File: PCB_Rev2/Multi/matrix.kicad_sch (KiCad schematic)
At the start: 126 parts

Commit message: Add ISO Support
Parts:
- added D54: DIODE, Diode_SMD:D_SOD-123, symbol Device:D
- added S54: MX1A, PCM_Switch_Keyboard_Hotswap_Kailh:SW_Hotswap_Kailh_MX_Plated_1.00u, symbol Switch:SW_Push
- S29: footprint PCM_Switch_Keyboard_Hotswap_Kailh:SW_Hotswap_Kailh_MX_Plated_1.75u -> PCM_Switch_Keyboard_Hotswap_Kailh:SW_Hotswap_Kailh_MX_Plated_1.75u_90deg
- S55, S56, S57, S60, S61, S62: footprint PCM_Switch_Keyboard_Hotswap_Kailh:SW_Hotswap_Kailh_MX_Plated_1.25u -> PCM_Switch_Keyboard_Hotswap_Kailh:SW_Hotswap_Kailh_MX_Plated_1.25u_90deg
- renumbered D54 to D55, D55 to D56, S54 to S55, S55 to S56
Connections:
- net col_11: now also S54.2
- net row_3: now also D54.1 (K)
- new net: D54.2 (A), S54.1
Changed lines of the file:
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@@
 	)
 	(junction
+		(at 332.74 125.73)
+		(diameter 0)
+		(color 0 0 0 0)
+	)
+	(junction
 		(at 332.74 60.96)
 		(diameter 0)
@@
 	)
 	(junction
+		(at 322.58 135.89)
+		(diameter 0)
+		(color 0 0 0 0)
+	)
+	(junction
 		(at 307.34 104.14)
 		(diameter 0)
@@
 	(wire
 		(pts
-			(xy 297.18 135.89) (xy 347.98 135.89)
+			(xy 297.18 135.89) (xy 322.58 135.89)
 		)
 		(stroke
@@
 	(wire
 		(pts
+			(xy 322.58 135.89) (xy 347.98 135.89)
+		)
+		(stroke
+			(width 0)
+			(type default)
+		)
+	)
+	(wire
+		(pts
 			(xy 205.74 60.96) (xy 205.74 82.55)
 		)
@@
 	(wire
 		(pts
-			(xy 332.74 104.14) (xy 332.74 147.32)
+			(xy 332.74 104.14) (xy 332.74 125.73)
 		)
 		(stroke
@@
 	(wire
 		(pts
+			(xy 322.58 134.62) (xy 322.58 135.89)
+		)
+		(stroke
+			(width 0)
+			(type default)
+		)
+	)
+	(wire
+		(pts
 			(xy 307.34 60.96) (xy 307.34 82.55)
 		)
@@
 	(wire
 		(pts
+			(xy 322.58 125.73) (xy 322.58 127)
+		)
+		(stroke
+			(width 0)
+			(type default)
+		)
+	)
+	(wire
+		(pts
 			(xy 322.58 71.12) (xy 347.98 71.12)
 		)
@@
 	(wire
 		(pts
+			(xy 332.74 125.73) (xy 332.74 147.32)
+		)
+		(stroke
+			(width 0)
+			(type default)
+		)
+	)
+	(wire
+		(pts
 			(xy 93.98 69.85) (xy 93.98 71.12)
 		)
@@
 			(project "PH60"
 				(path "/dca0f898-8fdb-4522-a51d-f4f4238906e7/dc5cd3b2-ef82-41de-b720-71645d542746"
-					(reference "D63")
+					(reference "D64")
 					(unit 1)
 				)
@@
 			(project "PH60"
 				(path "/dca0f898-8fdb-4522-a51d-f4f4238906e7/dc5cd3b2-ef82-41de-b720-71645d542746"
-					(reference "D57")
+					(reference "D58")
 					(unit 1)
 				)
@@
 			(project "PH60"
 				(path "/dca0f898-8fdb-4522-a51d-f4f4238906e7/dc5cd3b2-ef82-41de-b720-71645d542746"
-					(reference "D61")
+					(reference "D62")
 					(unit 1)
 				)
@@
 			(project "PH60"
 				(path "/dca0f898-8fdb-4522-a51d-f4f4238906e7/dc5cd3b2-ef82-41de-b720-71645d542746"
-					(reference "D59")
+					(reference "D60")
 					(unit 1)
 				)
@@
 			(project "PH60"
 				(path "/dca0f898-8fdb-4522-a51d-f4f4238906e7/dc5cd3b2-ef82-41de-b720-71645d542746"
-					(reference "S59")
+					(reference "S60")
 					(unit 1)
 				)
@@
 			)
 		)
-		(property "Footprint" "PCM_Switch_Keyboard_Hotswap_Kailh:SW_Hotswap_Kailh_MX_Plated_1.25u"
+		(property "Footprint" "PCM_Switch_Keyboard_Hotswap_Kailh:SW_Hotswap_Kailh_MX_Plated_1.25u_90deg"
 			(at 99.06 152.4 0)
 			(effects
@@
 			(project "PH60"
 				(path "/dca0f898-8fdb-4522-a51d-f4f4238906e7/dc5cd3b2-ef82-41de-b720-71645d542746"
-					(reference "S58")
+					(reference "S59")
 					(unit 1)
 				)
@@
 		(dnp no)
 		(fields_autoplaced yes)
-		(property "Reference" "S54"
+		(property "Reference" "S55"
 			(at 353.06 120.65 0)
 			(effects
@@
 			(project "PH60_Rev3"
 				(path "/dca0f898-8fdb-4522-a51d-f4f4238906e7/dc5cd3b2-ef82-41de-b720-71645d542746"
-					(reference "S54")
+					(reference "S55")
 					(unit 1)
 				)
@@
 			(project "PH60"
 				(path "/dca0f898-8fdb-4522-a51d-f4f4238906e7/dc5cd3b2-ef82-41de-b720-71645d542746"
-					(reference "D62")
+					(reference "D63")
 					(unit 1)
 				)
@@
 			)
 		)
-		(property "Footprint" "PCM_Switch_Keyboard_Hotswap_Kailh:SW_Hotswap_Kailh_MX_Plated_1.25u"
+		(property "Footprint" "PCM_Switch_Keyboard_Hotswap_Kailh:SW_Hotswap_Kailh_MX_Plated_1.25u_90deg"
 			(at 353.06 152.4 0)
 			(effects
@@
 			(project "PH60"
 				(path "/dca0f898-8fdb-4522-a51d-f4f4238906e7/dc5cd3b2-ef82-41de-b720-71645d542746"
-					(reference "S62")
+					(reference "S63")
 					(unit 1)
 				)
@@
 			(project "PH60"
 				(path "/dca0f898-8fdb-4522-a51d-f4f4238906e7/dc5cd3b2-ef82-41de-b720-71645d542746"
-					(reference "D60")
+					(reference "D61")
 					(unit 1)
 				)
@@
 			(project "PH60"
 				(path "/dca0f898-8fdb-4522-a51d-f4f4238906e7/dc5cd3b2-ef82-41de-b720-71645d542746"
-					(reference "S60")
+					(reference "S61")
 					(unit 1)
 				)
@@
 			)
 		)
-		(property "Footprint" "PCM_Switch_Keyboard_Hotswap_Kailh:SW_Hotswap_Kailh_MX_Plated_1.25u"
+		(property "Footprint" "PCM_Switch_Keyboard_Hotswap_Kailh:SW_Hotswap_Kailh_MX_Plated_1.25u_90deg"
 			(at 73.66 152.4 0)
 			(effects
@@
 			(project "PH60"
 				(path "/dca0f898-8fdb-4522-a51d-f4f4238906e7/dc5cd3b2-ef82-41de-b720-71645d542746"
-					(reference "S57")
+					(reference "S58")
 					(unit 1)
 				)
@@
 		(dnp no)
 		(fields_autoplaced yes)
-		(property "Reference" "D54"
+		(property "Reference" "D55"
 			(at 350.52 129.5399 90)
 			(effects
@@
 			(project "PH60_Rev3"
 				(path "/dca0f898-8fdb-4522-a51d-f4f4238906e7/dc5cd3b2-ef82-41de-b720-71645d542746"
-					(reference "D54")
+					(reference "D55")
 					(unit 1)
 				)
@@
 			)
 		)
-		(property "Footprint" "PCM_Switch_Keyboard_Hotswap_Kailh:SW_Hotswap_Kailh_MX_Plated_1.25u"
+		(property "Footprint" "PCM_Switch_Keyboard_Hotswap_Kailh:SW_Hotswap_Kailh_MX_Plated_1.25u_90deg"
 			(at 48.26 152.4 0)
 			(effects
@@
 			(project "PH60"
 				(path "/dca0f898-8fdb-4522-a51d-f4f4238906e7/dc5cd3b2-ef82-41de-b720-71645d542746"
-					(reference "S56")
+					(reference "S57")
 					(unit 1)
 				)
@@
 			)
 		)
-		(property "Footprint" "PCM_Switch_Keyboard_Hotswap_Kailh:SW_Hotswap_Kailh_MX_Plated_1.25u"
+		(property "Footprint" "PCM_Switch_Keyboard_Hotswap_Kailh:SW_Hotswap_Kailh_MX_Plated_1.25u_90deg"
 			(at 378.46 152.4 0)
 			(effects
@@
 			(project "PH60"
 				(path "/dca0f898-8fdb-4522-a51d-f4f4238906e7/dc5cd3b2-ef82-41de-b720-71645d542746"
-					(reference "S63")
+					(reference "S64")
 					(unit 1)
 				)
@@
 		(dnp no)
 		(fields_autoplaced yes)
-		(property "Reference" "S55"
+		(property "Reference" "S56"
 			(at 378.46 120.65 0)
 			(effects
@@
 			(project "PH60_Rev3"
 				(path "/dca0f898-8fdb-4522-a51d-f4f4238906e7/dc5cd3b2-ef82-41de-b720-71645d542746"
-					(reference "S55")
+					(reference "S56")
 					(unit 1)
 				)
@@
 			(project "PH60"
 				(path "/dca0f898-8fdb-4522-a51d-f4f4238906e7/dc5cd3b2-ef82-41de-b720-71645d542746"
-					(reference "D56")
+					(reference "D57")
 					(unit 1)
 				)
@@
 			)
 		)
-		(property "Footprint" "PCM_Switch_Keyboard_Hotswap_Kailh:SW_Hotswap_Kailh_MX_Plated_1.75u"
+		(property "Footprint" "PCM_Switch_Keyboard_Hotswap_Kailh:SW_Hotswap_Kailh_MX_Plated_1.75u_90deg"
 			(at 48.26 109.22 0)
 			(effects
@@
 			)
 		)
-		(property "Footprint" "PCM_Switch_Keyboard_Hotswap_Kailh:SW_Hotswap_Kailh_MX_Plated_1.25u"
+		(property "Footprint" "PCM_Switch_Keyboard_Hotswap_Kailh:SW_Hotswap_Kailh_MX_Plated_1.25u_90deg"
 			(at 327.66 152.4 0)
 			(effects
@@
 			(project "PH60"
 				(path "/dca0f898-8fdb-4522-a51d-f4f4238906e7/dc5cd3b2-ef82-41de-b720-71645d542746"
-					(reference "S61")
+					(reference "S62")
 					(unit 1)
 				)
@@
 		(dnp no)
 		(fields_autoplaced yes)
-		(property "Reference" "D55"
+		(property "Reference" "D56"
 			(at 375.92 129.5399 90)
 			(effects
@@
 			(project "PH60_Rev3"
 				(path "/dca0f898-8fdb-4522-a51d-f4f4238906e7/dc5cd3b2-ef82-41de-b720-71645d542746"
-					(reference "D55")
+					(reference "D56")
 					(unit 1)
 				)
@@
 			(project "PH60"
 				(path "/dca0f898-8fdb-4522-a51d-f4f4238906e7/dc5cd3b2-ef82-41de-b720-71645d542746"
-					(reference "D58")
+					(reference "D59")
+					(unit 1)
+				)
+			)
+		)
+	)
+	(symbol
+		(lib_id "Device:D")
+		(at 322.58 130.81 90)
+		(unit 1)
+		(exclude_from_sim no)
+		(in_bom yes)
+		(on_board yes)
+		(dnp no)
+		(fields_autoplaced yes)
+		(property "Reference" "D54"
+			(at 325.12 129.5399 90)
+			(effects
+				(font
+					(size 1.016 1.016)
+				)
+				(justify right)
+			)
+		)
+		(property "Value" "DIODE"
+			(at 325.12 132.0799 90)
+			(effects
+				(font
+					(size 1.016 1.016)
+				)
+				(justify right)
+			)
+		)
+		(property "Footprint" "Diode_SMD:D_SOD-123"
+			(at 322.58 130.81 0)
+			(effects
+				(font
+					(size 1.27 1.27)
+				)
+				(hide yes)
+			)
+		)
+		(property "Datasheet" "~"
+			(at 322.58 130.81 0)
+			(effects
+				(font
+					(size 1.27 1.27)
+				)
+				(hide yes)
+			)
+		)
+		(property "Description" "Diode"
+			(at 322.58 130.81 0)
+			(effects
+				(font
+					(size 1.27 1.27)
+				)
+				(hide yes)
+			)
+		)
+		(property "Sim.Device" "D"
+			(at 322.58 130.81 0)
+			(effects
+				(font
+					(size 1.27 1.27)
+				)
+				(hide yes)
+			)
+		)
+		(property "Sim.Pins" "1=K 2=A"
+			(at 322.58 130.81 0)
+			(effects
+				(font
+					(size 1.27 1.27)
+				)
+				(hide yes)
+			)
+		)
+		(pin "1"
+		)
+		(pin "2"
+		)
+		(instances
+			(project "PH60_Rev2"
+				(path "/dca0f898-8fdb-4522-a51d-f4f4238906e7/dc5cd3b2-ef82-41de-b720-71645d542746"
+					(reference "D54")
 					(unit 1)
 				)
@@
 					(unit 1)
 				)
+			)
+		)
+	)
+	(symbol
+		(lib_id "Switch:SW_Push")
+		(at 327.66 125.73 0)
+		(mirror x)
+		(unit 1)
+		(exclude_from_sim no)
+		(in_bom yes)
+		(on_board yes)
+		(dnp no)
+		(fields_autoplaced yes)
+		(property "Reference" "S54"
+			(at 327.66 120.65 0)
+			(effects
+				(font
+					(size 1.524 1.524)
+				)
+			)
+		)
+		(property "Value" "MX1A"
+			(at 327.66 123.19 0)
+			(effects
+				(font
+					(size 1.524 1.524)
+				)
+			)
+		)
+		(property "Footprint" "PCM_Switch_Keyboard_Hotswap_Kailh:SW_Hotswap_Kailh_MX_Plated_1.00u"
+			(at 327.66 130.81 0)
+			(effects
+				(font
+					(size 1.27 1.27)
+				)
+				(hide yes)
+			)
+		)
+		(property "Datasheet" "~"
+			(at 327.66 130.81 0)
+			(effects
+				(font
+					(size 1.27 1.27)
+				)
+				(hide yes)
+			)
+		)
+		(property "Description" "Push button switch, generic, two pins"
+			(at 327.66 125.73 0)
+			(effects
+				(font
+					(size 1.27 1.27)
+				)
+				(hide yes)
+			)
+		)
+		(pin "2"
+		)
+		(pin "1"
+		)
+		(instances
+			(project "PH60_Rev2"
+				(path "/dca0f898-8fdb-4522-a51d-f4f4238906e7/dc5cd3b2-ef82-41de-b720-71645d542746"
+					(reference "S54")
+					(unit 1)
+				)

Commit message: Wiring Improvement
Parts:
- S28: footprint PCM_Switch_Keyboard_Hotswap_Kailh:SW_Hotswap_Kailh_MX_Plated_1.50u -> PCM_Switch_Keyboard_Hotswap_Kailh:SW_Hotswap_Kailh_MX_Plated_1.50u_90deg
- S41: footprint PCM_Switch_Keyboard_Hotswap_Kailh:SW_Hotswap_Kailh_MX_Plated_2.25u -> PCM_Switch_Keyboard_Hotswap_Kailh:SW_Hotswap_Kailh_MX_Plated_2.25u_90deg
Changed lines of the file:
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@@
 			)
 		)
-		(property "Footprint" "PCM_Switch_Keyboard_Hotswap_Kailh:SW_Hotswap_Kailh_MX_Plated_1.50u"
+		(property "Footprint" "PCM_Switch_Keyboard_Hotswap_Kailh:SW_Hotswap_Kailh_MX_Plated_1.50u_90deg"
 			(at 378.46 87.63 0)
 			(effects
@@
 			)
 		)
-		(property "Footprint" "PCM_Switch_Keyboard_Hotswap_Kailh:SW_Hotswap_Kailh_MX_Plated_2.25u"
+		(property "Footprint" "PCM_Switch_Keyboard_Hotswap_Kailh:SW_Hotswap_Kailh_MX_Plated_2.25u_90deg"
 			(at 353.06 109.22 0)
 			(effects

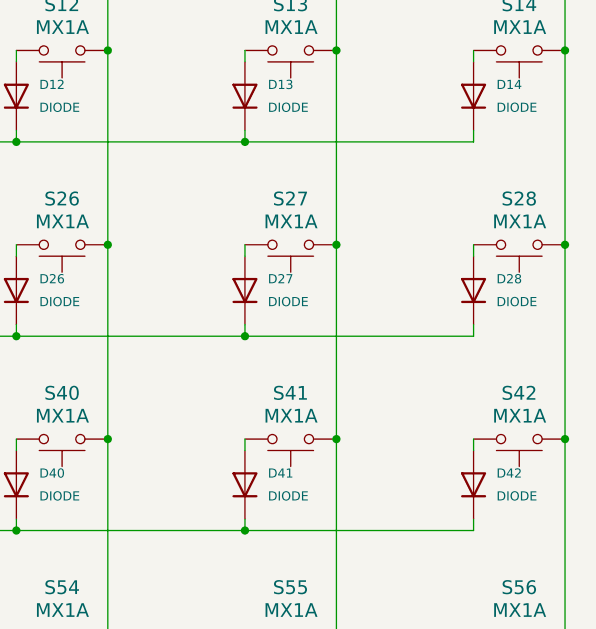
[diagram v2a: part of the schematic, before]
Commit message: Schematic Tinkering and RF Module Placing
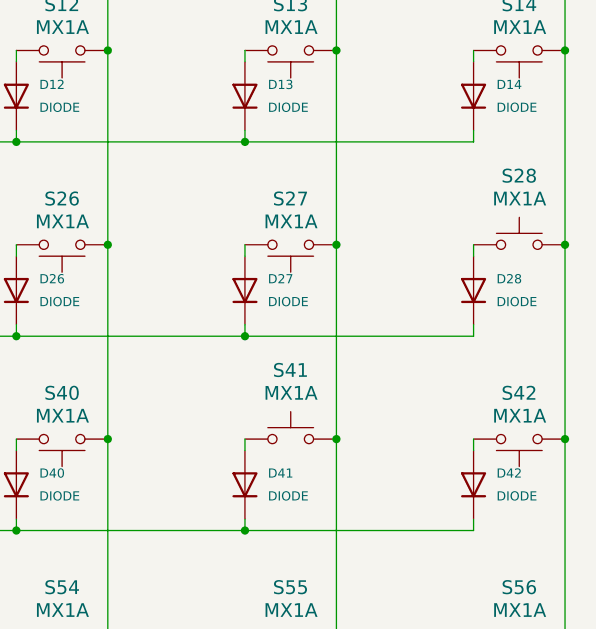
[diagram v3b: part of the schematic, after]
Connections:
- net col_12: now also S41.1; no longer S41.2
- net col_13: now also S28.1; no longer S28.2
- net at D28.2 (A): now also S28.2; no longer S28.1
- net at D41.2 (A): now also S41.2; no longer S41.1
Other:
- moved on the sheet: S28, S41
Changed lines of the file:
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@@
 	)
 	(junction
+		(at 383.54 82.55)
+		(diameter 0)
+		(color 0 0 0 0)
+	)
+	(junction
 		(at 271.78 135.89)
 		(diameter 0)
@@
 	)
 	(junction
+		(at 358.14 104.14)
+		(diameter 0)
+		(color 0 0 0 0)
+	)
+	(junction
 		(at 170.18 71.12)
 		(diameter 0)
@@
 	)
 	(junction
-		(at 383.54 82.55)
-		(diameter 0)
-		(color 0 0 0 0)
-	)
-	(junction
 		(at 347.98 135.89)
 		(diameter 0)
@@
 	)
 	(junction
-		(at 358.14 104.14)
-		(diameter 0)
-		(color 0 0 0 0)
-	)
-	(junction
 		(at 78.74 60.96)
 		(diameter 0)
@@
 	(wire
 		(pts
+			(xy 347.98 104.14) (xy 347.98 105.41)
+		)
+		(stroke
+			(width 0)
+			(type default)
+		)
+	)
+	(wire
+		(pts
 			(xy 43.18 69.85) (xy 43.18 71.12)
 		)
@@
 	(wire
 		(pts
-			(xy 358.14 82.55) (xy 358.14 104.14)
-		)
-		(stroke
-			(width 0)
-			(type default)
-		)
-	)
-	(wire
-		(pts
 			(xy 322.58 92.71) (xy 347.98 92.71)
 		)
@@
 	(wire
 		(pts
-			(xy 383.54 82.55) (xy 383.54 104.14)
-		)
-		(stroke
-			(width 0)
-			(type default)
-		)
-	)
-	(wire
-		(pts
 			(xy 144.78 114.3) (xy 170.18 114.3)
 		)
@@
 	(wire
 		(pts
-			(xy 373.38 82.55) (xy 373.38 83.82)
-		)
-		(stroke
-			(width 0)
-			(type default)
-		)
-	)
-	(wire
-		(pts
 			(xy 93.98 113.03) (xy 93.98 114.3)
 		)
@@
 	(wire
 		(pts
-			(xy 358.14 104.14) (xy 358.14 125.73)
+			(xy 358.14 82.55) (xy 358.14 104.14)
 		)
 		(stroke
@@
 	(wire
 		(pts
+			(xy 358.14 104.14) (xy 358.14 125.73)
+		)
+		(stroke
+			(width 0)
+			(type default)
+		)
+	)
+	(wire
+		(pts
+			(xy 373.38 82.55) (xy 373.38 83.82)
+		)
+		(stroke
+			(width 0)
+			(type default)
+		)
+	)
+	(wire
+		(pts
 			(xy 220.98 125.73) (xy 220.98 127)
 		)
@@
 	(wire
 		(pts
+			(xy 383.54 82.55) (xy 383.54 104.14)
+		)
+		(stroke
+			(width 0)
+			(type default)
+		)
+	)
+	(wire
+		(pts
 			(xy 271.78 104.14) (xy 271.78 105.41)
 		)
@@
 		)
 	)
-	(wire
-		(pts
-			(xy 347.98 104.14) (xy 347.98 105.41)
-		)
-		(stroke
-			(width 0)
-			(type default)
-		)
-	)
 	(global_label "row_0"
 		(shape input)
@@
 		(lib_id "Switch:SW_Push")
 		(at 378.46 82.55 0)
-		(mirror x)
+		(mirror y)
 		(unit 1)
 		(exclude_from_sim no)
@@
 		(fields_autoplaced yes)
 		(property "Reference" "S28"
-			(at 378.46 77.47 0)
+			(at 378.46 74.93 0)
 			(effects
 				(font
@@
 		)
 		(property "Value" "MX1A"
-			(at 378.46 80.01 0)
+			(at 378.46 77.47 0)
 			(effects
 				(font
@@
 		)
 		(property "Footprint" "PCM_Switch_Keyboard_Hotswap_Kailh:SW_Hotswap_Kailh_MX_Plated_1.50u_90deg"
-			(at 378.46 87.63 0)
+			(at 378.46 77.47 0)
 			(effects
 				(font
@@
 		)
 		(property "Datasheet" "~"
-			(at 378.46 87.63 0)
+			(at 378.46 77.47 0)
 			(effects
 				(font
@@
 		(lib_id "Switch:SW_Push")
 		(at 353.06 104.14 0)
-		(mirror x)
+		(mirror y)
 		(unit 1)
 		(exclude_from_sim no)
@@
 		(fields_autoplaced yes)
 		(property "Reference" "S41"
-			(at 353.06 99.06 0)
+			(at 353.06 96.52 0)
 			(effects
 				(font
@@
 		)
 		(property "Value" "MX1A"
-			(at 353.06 101.6 0)
+			(at 353.06 99.06 0)
 			(effects
 				(font
@@
 		)
 		(property "Footprint" "PCM_Switch_Keyboard_Hotswap_Kailh:SW_Hotswap_Kailh_MX_Plated_2.25u_90deg"
-			(at 353.06 109.22 0)
+			(at 353.06 99.06 0)
 			(effects
 				(font
@@
 		)
 		(property "Datasheet" "~"
-			(at 353.06 109.22 0)
+			(at 353.06 99.06 0)
 			(effects
 				(font

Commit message: Multi PCB Rework
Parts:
- added S14-2, S58-2, S63-2: MX1A, PCM_Switch_Keyboard_Hotswap_Kailh:SW_Hotswap_Kailh_MX_Plated_1.00u, symbol Switch:SW_Push
- added S28-2: MX1A, PCM_Switch_Keyboard_Hotswap_Kailh:SW_Hotswap_Kailh_MX_Plated_2.25u_90deg, symbol Switch:SW_Push
- added S29-2: MX1A, PCM_Switch_Keyboard_Hotswap_Kailh:SW_Hotswap_Kailh_MX_Plated_1.25u_90deg, symbol Switch:SW_Push
- added S41-2, S57-2, S59-2, S62-2, S64-2: MX1A, PCM_Switch_Keyboard_Hotswap_Kailh:SW_Hotswap_Kailh_MX_Plated_1.50u_90deg, symbol Switch:SW_Push
- added S43-2: MX1A, PCM_Switch_Keyboard_Hotswap_Kailh:SW_Hotswap_Kailh_MX_Plated_2.25u, symbol Switch:SW_Push
- added S55-2: MX1A, PCM_Switch_Keyboard_Hotswap_Kailh:SW_Hotswap_Kailh_MX_Plated_2.75u_90deg, symbol Switch:SW_Push
- added S60-2: MX1A, PCM_Switch_Keyboard_Hotswap_Kailh:SW_Hotswap_Kailh_MX_Plated_7.00u, symbol Switch:SW_Push
- S28: footprint PCM_Switch_Keyboard_Hotswap_Kailh:SW_Hotswap_Kailh_MX_Plated_1.50u_90deg -> PCM_Switch_Keyboard_Hotswap_Kailh:SW_Hotswap_Kailh_MX_Plated_ISOEnter_90deg
- S41: footprint PCM_Switch_Keyboard_Hotswap_Kailh:SW_Hotswap_Kailh_MX_Plated_2.25u_90deg -> PCM_Switch_Keyboard_Hotswap_Kailh:SW_Hotswap_Kailh_MX_Plated_1.00u
- S42: footprint PCM_Switch_Keyboard_Hotswap_Kailh:SW_Hotswap_Kailh_MX_Plated_2.25u -> PCM_Switch_Keyboard_Hotswap_Kailh:SW_Hotswap_Kailh_MX_Plated_1.25u
- S56: footprint PCM_Switch_Keyboard_Hotswap_Kailh:SW_Hotswap_Kailh_MX_Plated_2.75u_90deg -> PCM_Switch_Keyboard_Hotswap_Kailh:SW_Hotswap_Kailh_MX_Plated_1.00u
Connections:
- net col_0: now also S42.1, S29-2.1, S43-2.2, S57-2.1; no longer S42.2
- net col_1: now also S58-2.1
- net col_11: now also S62-2.1
- net col_12: now also S41.2, S41-2.1, S55-2.2, S63-2.1; no longer S41.1
- net col_13: now also S28.2, S14-2.2, S28-2.2, S64-2.1; no longer S28.1
- net col_2: now also S59-2.1
- net col_6: now also S60-2.1
- net at D62.2 (A), S62.1: now also S64-2.2
- net at D14.2 (A), S14.1: now also S14-2.1
- net at D56.2 (A), S56.1: now also S58-2.2
- net at D42.2 (A): now also S42.2, S43-2.1; no longer S42.1
- net at D60.2 (A), S60.1: now also S62-2.2
- net at D58.2 (A), S58.1: now also S60-2.2
- net at D28.2 (A): now also S28.1, S28-2.1; no longer S28.2
- net at D57.2 (A), S57.1: now also S59-2.2
- net at D55.2 (A), S55.1: now also S55-2.1
- net at D61.2 (A), S61.1: now also S63-2.2
- net at D55.2 (A), S55.1: now also S57-2.2
- net at D41.2 (A): now also S41.1, S41-2.2; no longer S41.2
- net at D29.2 (A), S29.1: now also S29-2.2
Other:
- moved on the sheet: S28, S41, S42

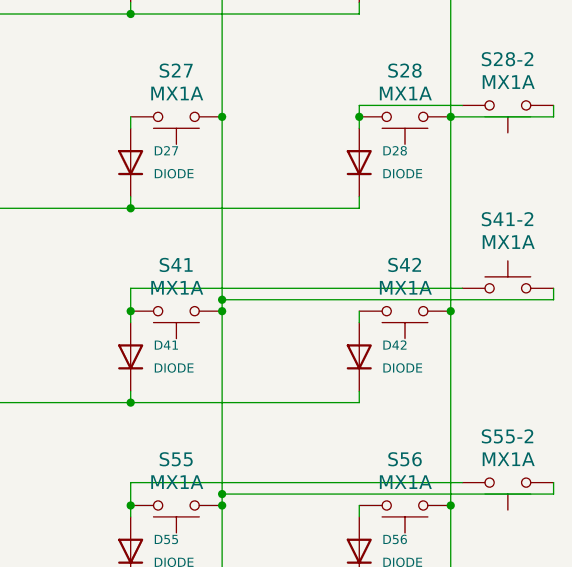
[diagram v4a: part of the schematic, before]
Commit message: Swap the Place of S42 and S14-2 on the PCB
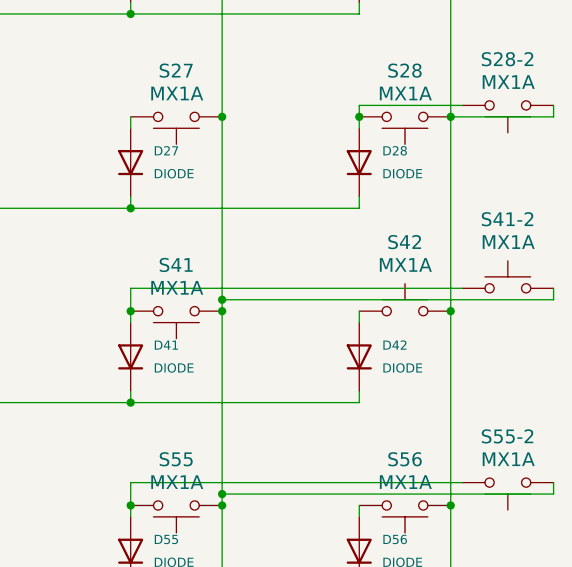
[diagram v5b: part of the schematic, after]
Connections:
- net col_13: now also S42.1; no longer S42.2
- net at D42.2 (A): now also S42.2; no longer S42.1
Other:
- moved on the sheet: S42
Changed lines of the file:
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@@
 	)
 	(junction
-		(at 383.54 104.14)
-		(diameter 0)
-		(color 0 0 0 0)
-	)
-	(junction
 		(at 358.14 102.87)
 		(diameter 0)
@@
 	)
 	(junction
+		(at 383.54 104.14)
+		(diameter 0)
+		(color 0 0 0 0)
+	)
+	(junction
 		(at 347.98 135.89)
 		(diameter 0)
@@
 	(wire
 		(pts
-			(xy 383.54 104.14) (xy 383.54 125.73)
-		)
-		(stroke
-			(width 0)
-			(type default)
-		)
-	)
-	(wire
-		(pts
 			(xy 271.78 60.96) (xy 271.78 62.23)
 		)
@@
 	(wire
 		(pts
+			(xy 383.54 104.14) (xy 383.54 125.73)
+		)
+		(stroke
+			(width 0)
+			(type default)
+		)
+	)
+	(wire
+		(pts
 			(xy 271.78 134.62) (xy 271.78 135.89)
 		)
@@
 		(lib_id "Switch:SW_Push")
 		(at 378.46 104.14 0)
-		(mirror x)
+		(mirror y)
 		(unit 1)
 		(exclude_from_sim no)
@@
 		(fields_autoplaced yes)
 		(property "Reference" "S42"
-			(at 378.46 99.06 0)
+			(at 378.46 96.52 0)
 			(effects
 				(font
@@
 		)
 		(property "Value" "MX1A"
-			(at 378.46 101.6 0)
+			(at 378.46 99.06 0)
 			(effects
 				(font
@@
 		)
 		(property "Footprint" "PCM_Switch_Keyboard_Hotswap_Kailh:SW_Hotswap_Kailh_MX_Plated_1.00u"
-			(at 378.46 109.22 0)
+			(at 378.46 99.06 0)
 			(effects
 				(font
@@
 		)
 		(property "Datasheet" "~"
-			(at 378.46 109.22 0)
+			(at 378.46 99.06 0)
 			(effects
 				(font
